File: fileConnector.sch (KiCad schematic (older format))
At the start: 13 parts, among them J6 TE_Eurocard_96pole, J9 Conn_01x02, U8 74AHC244, U9 74AHC244

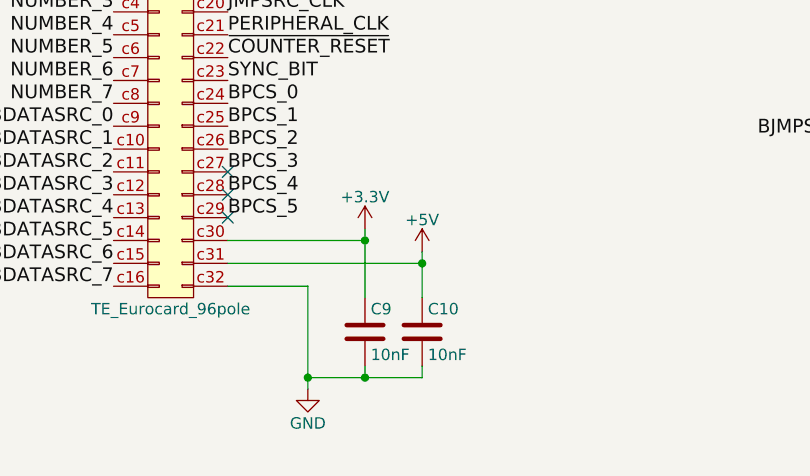
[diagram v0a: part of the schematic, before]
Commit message: V5.1 (#15)
* Remove compatibility for 5.0, 4.x and add 5.1+

* Fix switched pins on SN74LV393A #7

* Removed capacitor on 12V #11

* Add/Modify power decoupling capacitor #10

* Removing ADDSCR_CLK delay #9

* Schematics : set version 5.1, 2021 copyright and publish date

* Put non-electrolytic capacitor #10

* Set every capacitor size to 0805

* Add new footprint for J7 TE_3-641124-6 #6

* Schematic : set pinHeader on J12 #4

* Netlist, apply change to board, clean track, #6 #4 #12 #10

* Set version to 5.1, 2021 copyright and date, replace the missing QRcode

* Back the MM1 connectors #8

* Replace capacitor for U22 U23 U24 #13

* Better decoupling

* Increase version, year to 2021, clear status

* Precise the molex connector for power supply

* First step, import ses

* Clean bottom layer

* #14 Set the BWRITE2 bus instead of BWRITE1 on U12

* netlist, redo autorouting and cleaning

* use shields.io for colored badge

* Update gerbert files

* Changelog, updated BOM

* Small revision on blockDiagram

* Update README.md

* exporting pcb in pdf

* 3D images, diagram.png

* Update schematics pdf

* redo wavedrom_24bitsCounter
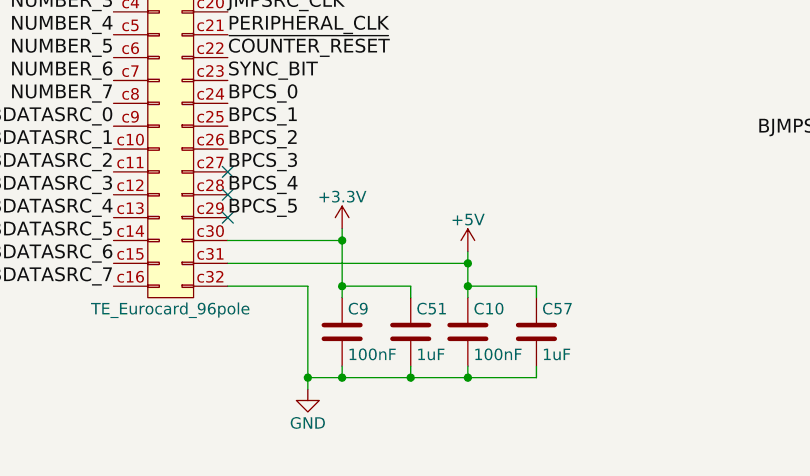
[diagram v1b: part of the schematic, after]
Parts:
- added C51, C57: 1uF, Capacitor_SMD:C_0805_2012Metric, symbol Device:C
- C10, C9: value 10nF -> 100nF
- J9: footprint Connector_PinSocket_2.54mm:PinSocket_1x02_P2.54mm_Vertical -> Connector_PinHeader_2.54mm:PinHeader_1x02_P2.54mm_Vertical
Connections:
- net +3V3: now also C51.1
- net +5V: now also C57.1
- net GND: now also C51.2, C57.2
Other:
- moved on the sheet: C10, C9
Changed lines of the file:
@@
 Sheet 3 10
 Title "GCM"
-Date "2020-11-23"
-Rev "V5.0"
+Date "2021-02-16"
+Rev "V5.1"
 Comp "Guillaume Guillet"
-Comment1 "Copyright Guillaume Guillet 2020"
+Comment1 "Copyright Guillaume Guillet 2021"
 Comment2 "Licensed under CERN-OHL-W v2 or later"
 Comment3 ""
@@
 L power:+5V #PWR059
 U 1 1 5B173077
-P 6100 6850
+P 6300 6850
 AR Path="/5B173077" Ref="#PWR059"  Part="1"
 AR Path="/5B31C462/5B173077" Ref="#PWR059"  Part="1"
-F 0 "#PWR059" H 6100 6700 50  0001 C CNN
-F 1 "+5V" H 6100 6990 50  0000 C CNN
-F 2 "" H 6100 6850 50  0001 C CNN
-F 3 "" H 6100 6850 50  0001 C CNN
-	1    6100 6850
+F 0 "#PWR059" H 6300 6700 50  0001 C CNN
+F 1 "+5V" H 6300 6990 50  0000 C CNN
+F 2 "" H 6300 6850 50  0001 C CNN
+F 3 "" H 6300 6850 50  0001 C CNN
+	1    6300 6850
 	1    0    0    -1
 $EndComp
@@
 L power:+3V3 #PWR060
 U 1 1 5B0EADF6
-P 5850 6750
+P 5750 6750
 AR Path="/5B0EADF6" Ref="#PWR060"  Part="1"
 AR Path="/5B31C462/5B0EADF6" Ref="#PWR060"  Part="1"
-F 0 "#PWR060" H 5850 6600 50  0001 C CNN
-F 1 "+3.3V" H 5850 6890 50  0000 C CNN
-F 2 "" H 5850 6750 50  0001 C CNN
-F 3 "" H 5850 6750 50  0001 C CNN
-	1    5850 6750
+F 0 "#PWR060" H 5750 6600 50  0001 C CNN
+F 1 "+3.3V" H 5750 6890 50  0000 C CNN
+F 2 "" H 5750 6750 50  0001 C CNN
+F 3 "" H 5750 6750 50  0001 C CNN
+	1    5750 6750
 	1    0    0    -1
 $EndComp
@@
 L Device:C C9
 U 1 1 5B0EB326
-P 5850 7200
+P 5750 7200
 AR Path="/5B0EB326" Ref="C9"  Part="1"
 AR Path="/5B31C462/5B0EB326" Ref="C9"  Part="1"
-F 0 "C9" H 5875 7300 50  0000 L CNN
-F 1 "10nF" H 5875 7100 50  0000 L CNN
-F 2 "Capacitor_SMD:C_0805_2012Metric" H 5888 7050 50  0001 C CNN
-F 3 "" H 5850 7200 50  0001 C CNN
-	1    5850 7200
+F 0 "C9" H 5775 7300 50  0000 L CNN
+F 1 "100nF" H 5775 7100 50  0000 L CNN
+F 2 "Capacitor_SMD:C_0805_2012Metric" H 5788 7050 50  0001 C CNN
+F 3 "" H 5750 7200 50  0001 C CNN
+	1    5750 7200
 	1    0    0    -1
 $EndComp
@@
 L Device:C C10
 U 1 1 5B0EB41C
-P 6100 7200
+P 6300 7200
 AR Path="/5B0EB41C" Ref="C10"  Part="1"
 AR Path="/5B31C462/5B0EB41C" Ref="C10"  Part="1"
-F 0 "C10" H 6125 7300 50  0000 L CNN
-F 1 "10nF" H 6125 7100 50  0000 L CNN
-F 2 "Capacitor_SMD:C_0805_2012Metric" H 6138 7050 50  0001 C CNN
-F 3 "" H 6100 7200 50  0001 C CNN
-	1    6100 7200
+F 0 "C10" H 6325 7300 50  0000 L CNN
+F 1 "100nF" H 6325 7100 50  0000 L CNN
+F 2 "Capacitor_SMD:C_0805_2012Metric" H 6338 7050 50  0001 C CNN
+F 3 "" H 6300 7200 50  0001 C CNN
+	1    6300 7200
 	1    0    0    -1
 $EndComp
@@
 	5250 7000 5600 7000
 Wire Wire Line
-	6100 6850 6100 6900
-Wire Wire Line
-	5600 7400 5850 7400
-Wire Wire Line
-	5850 7400 5850 7350
+	6300 6850 6300 6900
 Connection ~ 5600 7400
-Wire Wire Line
-	6100 7400 6100 7350
-Connection ~ 5850 7400
-Wire Wire Line
-	5850 6750 5850 6800
-Wire Wire Line
-	5250 6900 6100 6900
-Connection ~ 6100 6900
-Wire Wire Line
-	5250 6800 5850 6800
-Connection ~ 5850 6800
+Connection ~ 6300 6900
 Text Label 3050 1250 2    60   ~ 0
 BREAD1_0
@@
 	5600 7400 5600 7450
 Wire Wire Line
-	5850 7400 6100 7400
-Wire Wire Line
-	6100 6900 6100 7050
-Wire Wire Line
-	5850 6800 5850 7050
+	6300 6900 6300 7000
 Wire Wire Line
 	2300 3600 2300 3650
@@
 F 0 "J9" H 6930 1292 50  0000 L CNN
 F 1 "Conn_01x02" H 6930 1201 50  0000 L CNN
-F 2 "Connector_PinSocket_2.54mm:PinSocket_1x02_P2.54mm_Vertical" H 6850 1300 50  0001 C CNN
+F 2 "Connector_PinHeader_2.54mm:PinHeader_1x02_P2.54mm_Vertical" H 6850 1300 50  0001 C CNN
 F 3 "~" H 6850 1300 50  0001 C CNN
 	1    6850 1300
@@
 	1    0    0    -1
 $EndComp
+$Comp
+L Device:C C?
+U 1 1 602EDA53
+P 6050 7200
+AR Path="/602EDA53" Ref="C?"  Part="1"
+AR Path="/5B31C462/602EDA53" Ref="C51"  Part="1"
+F 0 "C51" H 6075 7300 50  0000 L CNN
+F 1 "1uF" H 6075 7100 50  0000 L CNN
+F 2 "Capacitor_SMD:C_0805_2012Metric" H 6088 7050 50  0001 C CNN
+F 3 "" H 6050 7200 50  0001 C CNN
+	1    6050 7200
+	1    0    0    -1
+$EndComp
+Wire Wire Line
+	5750 6750 5750 6800
+Wire Wire Line
+	5250 6800 5750 6800
+Connection ~ 5750 6800
+Wire Wire Line
+	5750 6800 5750 7000
+$Comp
+L Device:C C?
+U 1 1 6033559A
+P 6600 7200
+AR Path="/6033559A" Ref="C?"  Part="1"
+AR Path="/5B31C462/6033559A" Ref="C57"  Part="1"
+F 0 "C57" H 6625 7300 50  0000 L CNN
+F 1 "1uF" H 6625 7100 50  0000 L CNN
+F 2 "Capacitor_SMD:C_0805_2012Metric" H 6638 7050 50  0001 C CNN
+F 3 "" H 6600 7200 50  0001 C CNN
+	1    6600 7200
+	1    0    0    -1
+$EndComp
+Wire Wire Line
+	6600 7400 6600 7350
+Wire Wire Line
+	6300 7350 6300 7400
+Connection ~ 6300 7400
+Wire Wire Line
+	6300 7400 6600 7400
+Wire Wire Line
+	6050 7400 6050 7350
+Wire Wire Line
+	6050 7400 6300 7400
+Connection ~ 6050 7400
+Wire Wire Line
+	5600 7400 5750 7400
+Wire Wire Line
+	5750 7400 5750 7350
+Connection ~ 5750 7400
+Wire Wire Line
+	5750 7400 6050 7400
+Wire Wire Line
+	5250 6900 6300 6900
+Wire Wire Line
+	6050 7050 6050 7000
+Wire Wire Line
+	6050 7000 5750 7000
+Connection ~ 5750 7000
+Wire Wire Line
+	5750 7000 5750 7050
+Wire Wire Line
+	6600 7050 6600 7000
+Wire Wire Line
+	6600 7000 6300 7000
 Wire Bus Line
 	10050 4950 10050 5550
@@
 Wire Bus Line
 	8250 4000 8250 6350
+Connection ~ 6300 7000
+Wire Wire Line
+	6300 7000 6300 7050
 $EndSCHEMATC
